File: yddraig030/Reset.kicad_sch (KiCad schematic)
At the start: 22 parts, among them J1301 ExtReset, J1302 Ext RUN LED, Q1301 2N4403, Q1302 2N4403, Q1303 2N4403, SW1301 Reset, U1301 NE555P

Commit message: ddraig030 schematic done
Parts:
- renumbered C1301 to C201, C1302 to C202, C1303 to C203, D1301 to D201, D1302 to D202, D1303 to D203, J1301 to J201, J1302 to J202, Q1301 to Q201, Q1302 to Q202, Q1303 to Q203, R1301 to R201, R1302 to R202, R1303 to R203, R1304 to R204, R1305 to R205, R1306 to R206, R1307 to R207, R1308 to R208, R1309 to R209, SW1301 to SW201, U1301 to U201

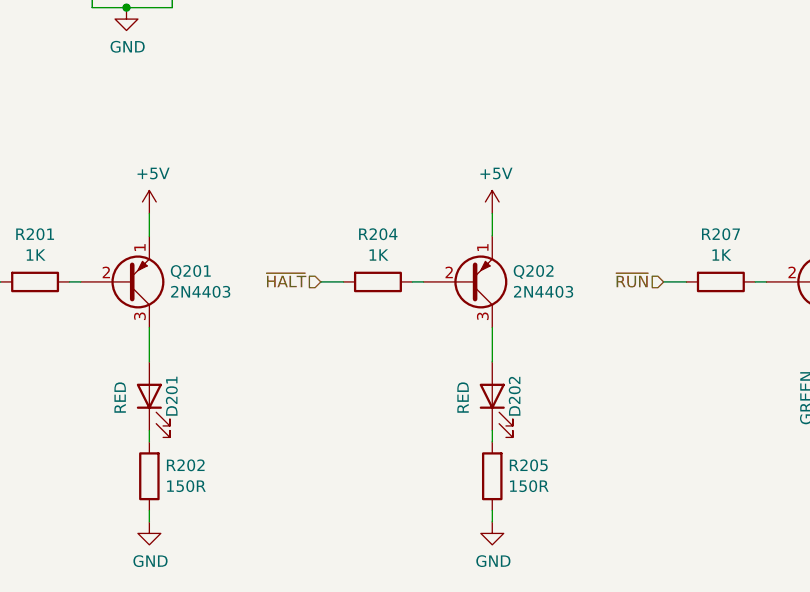
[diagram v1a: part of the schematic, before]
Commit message: yddraig030: Fixed ERC check errors
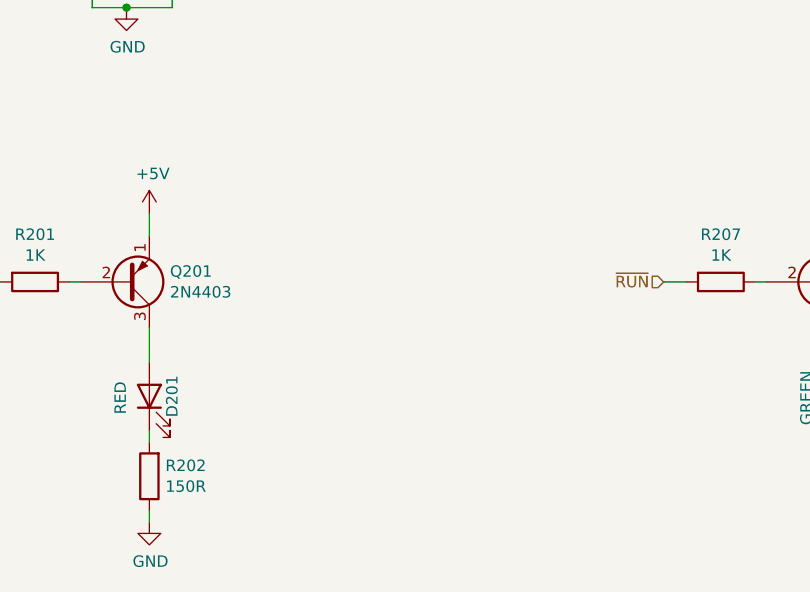
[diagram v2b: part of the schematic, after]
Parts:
- removed D202: RED, LED_THT:LED_D5.0mm, symbol Device:LED
- removed Q202: 2N4403, Package_TO_SOT_THT:TO-92, symbol Device:Q_PNP_EBC
- removed R204: 1K, Resistor_THT:R_Axial_DIN0207_L6.3mm_D2.5mm_P10.16mm_Horizontal, symbol Device:R
- removed R205: 150R, Resistor_THT:R_Axial_DIN0207_L6.3mm_D2.5mm_P10.16mm_Horizontal, symbol Device:R
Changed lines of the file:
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@@
-    (stroke (width 0) (type default) (color 0 0 0 0))
-  )
-  (wire (pts (xy 133.35 113.03) (xy 133.35 115.57))
     (stroke (width 0) (type default) (color 0 0 0 0))
   )
@@
     (stroke (width 0) (type default) (color 0 0 0 0))
   )
-  (wire (pts (xy 133.35 125.73) (xy 133.35 129.54))
-    (stroke (width 0) (type default) (color 0 0 0 0))
-  )
   (wire (pts (xy 135.89 77.47) (xy 152.4 77.47))
     (stroke (width 0) (type default) (color 0 0 0 0))
@@
     (stroke (width 0) (type default) (color 0 0 0 0))
   )
-  (wire (pts (xy 133.35 137.16) (xy 133.35 138.43))
-    (stroke (width 0) (type default) (color 0 0 0 0))
-  )
   (wire (pts (xy 95.25 125.73) (xy 95.25 129.54))
     (stroke (width 0) (type default) (color 0 0 0 0))
   )
-  (wire (pts (xy 114.3 120.65) (xy 116.84 120.65))
-    (stroke (width 0) (type default) (color 0 0 0 0))
-  )
   (wire (pts (xy 87.63 82.55) (xy 88.9 82.55))
     (stroke (width 0) (type default) (color 0 0 0 0))
@@
     (stroke (width 0) (type default) (color 0 0 0 0))
   )
-  (wire (pts (xy 124.46 120.65) (xy 125.73 120.65))
-    (stroke (width 0) (type default) (color 0 0 0 0))
-  )
   (wire (pts (xy 118.11 58.42) (xy 118.11 67.31))
     (stroke (width 0) (type default) (color 0 0 0 0))
@@
     (stroke (width 0) (type default) (color 0 0 0 0))
   )
-  (wire (pts (xy 133.35 146.05) (xy 133.35 147.32))
-    (stroke (width 0) (type default) (color 0 0 0 0))
-  )
   (wire (pts (xy 95.25 146.05) (xy 95.25 147.32))
     (stroke (width 0) (type default) (color 0 0 0 0))
-  )
-  (hierarchical_label "~{HALT}" (shape input) (at 114.3 120.65 180)
-    (effects (font (size 1.27 1.27)) (justify right))
   )
   (hierarchical_label "~{RUN}" (shape input) (at 152.4 120.65 180)
@@
       (effects (font (size 1.27 1.27)) hide)
     )
-    (pin "1")
-  )
-  (symbol (lib_id "Device:R") (at 120.65 120.65 270) (unit 1)
-    (in_bom yes) (on_board yes)
-    (property "Reference" "R204" (id 0) (at 120.65 115.3922 90))
-    (property "Value" "1K" (id 1) (at 120.65 117.7036 90))
-    (property "Footprint" "Resistor_THT:R_Axial_DIN0207_L6.3mm_D2.5mm_P10.16mm_Horizontal" (id 2) (at 120.65 118.872 90)
-      (effects (font (size 1.27 1.27)) hide)
-    )
-    (property "Datasheet" "~" (id 3) (at 120.65 120.65 0)
-      (effects (font (size 1.27 1.27)) hide)
-    )
-    (pin "1")
-    (pin "2")
-  )
-  (symbol (lib_id "Device:R") (at 133.35 142.24 180) (unit 1)
-    (in_bom yes) (on_board yes)
-    (property "Reference" "R205" (id 0) (at 135.128 141.0716 0)
-      (effects (font (size 1.27 1.27)) (justify right))
-    )
-    (property "Value" "150R" (id 1) (at 135.128 143.383 0)
-      (effects (font (size 1.27 1.27)) (justify right))
-    )
-    (property "Footprint" "Resistor_THT:R_Axial_DIN0207_L6.3mm_D2.5mm_P10.16mm_Horizontal" (id 2) (at 135.128 142.24 90)
-      (effects (font (size 1.27 1.27)) hide)
-    )
-    (property "Datasheet" "~" (id 3) (at 133.35 142.24 0)
-      (effects (font (size 1.27 1.27)) hide)
-    )
-    (pin "1")
-    (pin "2")
-  )
-  (symbol (lib_id "Device:Q_PNP_EBC") (at 130.81 120.65 0) (mirror x) (unit 1)
-    (in_bom yes) (on_board yes)
-    (property "Reference" "Q202" (id 0) (at 135.636 119.4816 0)
-      (effects (font (size 1.27 1.27)) (justify left))
-    )
-    (property "Value" "2N4403" (id 1) (at 135.636 121.793 0)
-      (effects (font (size 1.27 1.27)) (justify left))
-    )
-    (property "Footprint" "Package_TO_SOT_THT:TO-92" (id 2) (at 135.89 123.19 0)
-      (effects (font (size 1.27 1.27)) hide)
-    )
-    (property "Datasheet" "~" (id 3) (at 130.81 120.65 0)
-      (effects (font (size 1.27 1.27)) hide)
-    )
-    (pin "1")
-    (pin "2")
-    (pin "3")
-  )
-  (symbol (lib_id "Device:LED") (at 133.35 133.35 90) (unit 1)
-    (in_bom yes) (on_board yes)
-    (property "Reference" "D202" (id 0) (at 135.89 133.35 0))
-    (property "Value" "RED" (id 1) (at 130.1496 133.5278 0))
-    (property "Footprint" "LED_THT:LED_D5.0mm" (id 2) (at 133.35 133.35 0)
-      (effects (font (size 1.27 1.27)) hide)
-    )
-    (property "Datasheet" "~" (id 3) (at 133.35 133.35 0)
-      (effects (font (size 1.27 1.27)) hide)
-    )
-    (pin "1")
-    (pin "2")
-  )
-  (symbol (lib_id "power:GND") (at 133.35 147.32 0) (unit 1)
-    (in_bom yes) (on_board yes)
-    (property "Reference" "#PWR0205" (id 0) (at 133.35 153.67 0)
-      (effects (font (size 1.27 1.27)) hide)
-    )
-    (property "Value" "GND" (id 1) (at 133.477 151.7142 0))
-    (property "Footprint" "" (id 2) (at 133.35 147.32 0)
-      (effects (font (size 1.27 1.27)) hide)
-    )
-    (property "Datasheet" "" (id 3) (at 133.35 147.32 0)
-      (effects (font (size 1.27 1.27)) hide)
-    )
-    (pin "1")
-  )
-  (symbol (lib_id "power:+5V") (at 133.35 113.03 0) (unit 1)
-    (in_bom yes) (on_board yes)
-    (property "Reference" "#PWR0204" (id 0) (at 133.35 116.84 0)
-      (effects (font (size 1.27 1.27)) hide)
-    )
-    (property "Value" "+5V" (id 1) (at 133.731 108.6358 0))
-    (property "Footprint" "" (id 2) (at 133.35 113.03 0)
-      (effects (font (size 1.27 1.27)) hide)
-    )
-    (property "Datasheet" "" (id 3) (at 133.35 113.03 0)
-      (effects (font (size 1.27 1.27)) hide)
-    )

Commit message: Started PCB layout
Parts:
- renumbered D203 to D202, Q203 to Q202, R206 to R204, R207 to R205, R208 to R206, R209 to R207
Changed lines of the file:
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@@
   (symbol (lib_id "Device:R") (at 158.75 58.42 0) (unit 1)
     (in_bom yes) (on_board yes)
-    (property "Reference" "R206" (id 0) (at 160.528 57.2516 0)
+    (property "Reference" "R204" (id 0) (at 160.528 57.2516 0)
       (effects (font (size 1.27 1.27)) (justify left))
     )
@@
   (symbol (lib_id "power:GND") (at 135.89 80.01 0) (unit 1)
     (in_bom yes) (on_board yes)
-    (property "Reference" "#PWR0207" (id 0) (at 135.89 86.36 0)
+    (property "Reference" "#PWR0205" (id 0) (at 135.89 86.36 0)
       (effects (font (size 1.27 1.27)) hide)
     )
@@
   (symbol (lib_id "power:+5V") (at 135.89 43.18 0) (unit 1)
     (in_bom yes) (on_board yes)
-    (property "Reference" "#PWR0206" (id 0) (at 135.89 46.99 0)
+    (property "Reference" "#PWR0204" (id 0) (at 135.89 46.99 0)
       (effects (font (size 1.27 1.27)) hide)
     )
@@
   (symbol (lib_id "Device:R") (at 158.75 120.65 270) (unit 1)
     (in_bom yes) (on_board yes)
-    (property "Reference" "R207" (id 0) (at 158.75 115.3922 90))
+    (property "Reference" "R205" (id 0) (at 158.75 115.3922 90))
     (property "Value" "1K" (id 1) (at 158.75 117.7036 90))
     (property "Footprint" "Resistor_THT:R_Axial_DIN0207_L6.3mm_D2.5mm_P10.16mm_Horizontal" (id 2) (at 158.75 118.872 90)
@@
   (symbol (lib_id "Device:R") (at 171.45 142.24 180) (unit 1)
     (in_bom yes) (on_board yes)
-    (property "Reference" "R208" (id 0) (at 173.228 141.0716 0)
+    (property "Reference" "R206" (id 0) (at 173.228 141.0716 0)
       (effects (font (size 1.27 1.27)) (justify right))
     )
@@
   (symbol (lib_id "Device:Q_PNP_EBC") (at 168.91 120.65 0) (mirror x) (unit 1)
     (in_bom yes) (on_board yes)
-    (property "Reference" "Q203" (id 0) (at 173.736 119.4816 0)
+    (property "Reference" "Q202" (id 0) (at 173.736 119.4816 0)
       (effects (font (size 1.27 1.27)) (justify left))
     )
@@
   (symbol (lib_id "Device:LED") (at 171.45 133.35 90) (unit 1)
     (in_bom yes) (on_board yes)
-    (property "Reference" "D203" (id 0) (at 173.99 133.35 0))
+    (property "Reference" "D202" (id 0) (at 173.99 133.35 0))
     (property "Value" "GREEN" (id 1) (at 168.2496 133.5278 0))
     (property "Footprint" "LED_THT:LED_D5.0mm" (id 2) (at 171.45 133.35 0)
@@
   (symbol (lib_id "power:GND") (at 171.45 147.32 0) (unit 1)
     (in_bom yes) (on_board yes)
-    (property "Reference" "#PWR0209" (id 0) (at 171.45 153.67 0)
+    (property "Reference" "#PWR0207" (id 0) (at 171.45 153.67 0)
       (effects (font (size 1.27 1.27)) hide)
     )
@@
   (symbol (lib_id "power:+5V") (at 171.45 113.03 0) (unit 1)
     (in_bom yes) (on_board yes)
-    (property "Reference" "#PWR0208" (id 0) (at 171.45 116.84 0)
+    (property "Reference" "#PWR0206" (id 0) (at 171.45 116.84 0)
       (effects (font (size 1.27 1.27)) hide)
     )
@@
   (symbol (lib_id "Device:R") (at 184.15 142.24 180) (unit 1)
     (in_bom yes) (on_board yes)
-    (property "Reference" "R209" (id 0) (at 185.928 141.0716 0)
+    (property "Reference" "R207" (id 0) (at 185.928 141.0716 0)
       (effects (font (size 1.27 1.27)) (justify right))
     )
@@
   (symbol (lib_id "power:GND") (at 184.15 147.32 0) (unit 1)
     (in_bom yes) (on_board yes)
-    (property "Reference" "#PWR0210" (id 0) (at 184.15 153.67 0)
-      (effects (font (size 1.27 1.27)) hide)
-    )
+    (property "Reference" "#PWR0208" (id 0) (at 184.15 153.67 0)
+      (effects (font (size 1.27 1.27)) hide)
+    )

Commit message: Working on PCB layout
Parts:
- C201, C203: footprint Capacitor_THT:CP_Radial_D5.0mm_P2.50mm -> Capacitor_SMD:CP_Elec_4x5.3
- C202: footprint Capacitor_THT:C_Disc_D3.8mm_W2.6mm_P2.50mm -> Capacitor_SMD:C_0805_2012Metric
- D201, D202: footprint LED_THT:LED_D5.0mm -> LED_SMD:LED_1206_3216Metric
- R201, R202, R203, R204, R205, R206, R207: footprint Resistor_THT:R_Axial_DIN0207_L6.3mm_D2.5mm_P10.16mm_Horizontal -> Resistor_SMD:R_0805_2012Metric
- U201: footprint Package_DIP:DIP-8_W7.62mm -> Package_SO:SO-8_3.9x4.9mm_P1.27mm
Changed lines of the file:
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@@
     (property "Reference" "U201" (id 0) (at 130.81 48.26 0))
     (property "Value" "NE555P" (id 1) (at 140.97 48.26 0))
-    (property "Footprint" "Package_DIP:DIP-8_W7.62mm" (id 2) (at 152.4 68.58 0)
+    (property "Footprint" "Package_SO:SO-8_3.9x4.9mm_P1.27mm" (id 2) (at 152.4 68.58 0)
       (effects (font (size 1.27 1.27)) hide)
     )
@@
       (effects (font (size 1.27 1.27)) (justify left))
     )
-    (property "Footprint" "Resistor_THT:R_Axial_DIN0207_L6.3mm_D2.5mm_P10.16mm_Horizontal" (id 2) (at 104.902 58.42 90)
+    (property "Footprint" "Resistor_SMD:R_0805_2012Metric" (id 2) (at 104.902 58.42 90)
       (effects (font (size 1.27 1.27)) hide)
     )
@@
       (effects (font (size 1.27 1.27)) (justify left))
     )
-    (property "Footprint" "Resistor_THT:R_Axial_DIN0207_L6.3mm_D2.5mm_P10.16mm_Horizontal" (id 2) (at 156.972 58.42 90)
+    (property "Footprint" "Resistor_SMD:R_0805_2012Metric" (id 2) (at 156.972 58.42 90)
       (effects (font (size 1.27 1.27)) hide)
     )
@@
       (effects (font (size 1.27 1.27)) (justify left))
     )
-    (property "Footprint" "Capacitor_THT:CP_Radial_D5.0mm_P2.50mm" (id 2) (at 153.3652 74.93 0)
+    (property "Footprint" "Capacitor_SMD:CP_Elec_4x5.3" (id 2) (at 153.3652 74.93 0)
       (effects (font (size 1.27 1.27)) hide)
     )
@@
       (effects (font (size 1.27 1.27)) (justify left))
     )
-    (property "Footprint" "Capacitor_THT:CP_Radial_D5.0mm_P2.50mm" (id 2) (at 107.6452 74.93 0)
+    (property "Footprint" "Capacitor_SMD:CP_Elec_4x5.3" (id 2) (at 107.6452 74.93 0)
       (effects (font (size 1.27 1.27)) hide)
     )
@@
       (effects (font (size 1.27 1.27)) (justify left))
     )
-    (property "Footprint" "Capacitor_THT:C_Disc_D3.8mm_W2.6mm_P2.50mm" (id 2) (at 119.0752 74.93 0)
+    (property "Footprint" "Capacitor_SMD:C_0805_2012Metric" (id 2) (at 119.0752 74.93 0)
       (effects (font (size 1.27 1.27)) hide)
     )
@@
     (property "Reference" "R201" (id 0) (at 82.55 115.3922 90))
     (property "Value" "1K" (id 1) (at 82.55 117.7036 90))
-    (property "Footprint" "Resistor_THT:R_Axial_DIN0207_L6.3mm_D2.5mm_P10.16mm_Horizontal" (id 2) (at 82.55 118.872 90)
+    (property "Footprint" "Resistor_SMD:R_0805_2012Metric" (id 2) (at 82.55 118.872 90)
       (effects (font (size 1.27 1.27)) hide)
     )
@@
       (effects (font (size 1.27 1.27)) (justify right))
     )
-    (property "Footprint" "Resistor_THT:R_Axial_DIN0207_L6.3mm_D2.5mm_P10.16mm_Horizontal" (id 2) (at 97.028 142.24 90)
+    (property "Footprint" "Resistor_SMD:R_0805_2012Metric" (id 2) (at 97.028 142.24 90)
       (effects (font (size 1.27 1.27)) hide)
     )
@@
     (property "Reference" "D201" (id 0) (at 97.79 133.35 0))
     (property "Value" "RED" (id 1) (at 92.0496 133.5278 0))
-    (property "Footprint" "LED_THT:LED_D5.0mm" (id 2) (at 95.25 133.35 0)
+    (property "Footprint" "LED_SMD:LED_1206_3216Metric" (id 2) (at 95.25 133.35 0)
       (effects (font (size 1.27 1.27)) hide)
     )
@@
     (property "Reference" "R205" (id 0) (at 158.75 115.3922 90))
     (property "Value" "1K" (id 1) (at 158.75 117.7036 90))
-    (property "Footprint" "Resistor_THT:R_Axial_DIN0207_L6.3mm_D2.5mm_P10.16mm_Horizontal" (id 2) (at 158.75 118.872 90)
+    (property "Footprint" "Resistor_SMD:R_0805_2012Metric" (id 2) (at 158.75 118.872 90)
       (effects (font (size 1.27 1.27)) hide)
     )
@@
       (effects (font (size 1.27 1.27)) (justify right))
     )
-    (property "Footprint" "Resistor_THT:R_Axial_DIN0207_L6.3mm_D2.5mm_P10.16mm_Horizontal" (id 2) (at 173.228 142.24 90)
+    (property "Footprint" "Resistor_SMD:R_0805_2012Metric" (id 2) (at 173.228 142.24 90)
       (effects (font (size 1.27 1.27)) hide)
     )
@@
     (property "Reference" "D202" (id 0) (at 173.99 133.35 0))
     (property "Value" "GREEN" (id 1) (at 168.2496 133.5278 0))
-    (property "Footprint" "LED_THT:LED_D5.0mm" (id 2) (at 171.45 133.35 0)
+    (property "Footprint" "LED_SMD:LED_1206_3216Metric" (id 2) (at 171.45 133.35 0)
       (effects (font (size 1.27 1.27)) hide)
     )
@@
       (effects (font (size 1.27 1.27)) (justify right))
     )
-    (property "Footprint" "Resistor_THT:R_Axial_DIN0207_L6.3mm_D2.5mm_P10.16mm_Horizontal" (id 2) (at 185.928 142.24 90)
-      (effects (font (size 1.27 1.27)) hide)
-    )
+    (property "Footprint" "Resistor_SMD:R_0805_2012Metric" (id 2) (at 185.928 142.24 90)
+      (effects (font (size 1.27 1.27)) hide)
+    )

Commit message: Some more changes to SMD version
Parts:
- removed Q201, Q202: 2N4403, Package_TO_SOT_THT:TO-92, symbol Device:Q_PNP_EBC
- added Q201, Q202: BC858, Package_TO_SOT_SMD:SOT-23, symbol Transistor_BJT:BC858
- U201: footprint Package_SO:SO-8_3.9x4.9mm_P1.27mm -> Package_SO:SO-8_5.3x6.2mm_P1.27mm
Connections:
- net +5V: now also Q201.2 (E), Q202.2 (E)
- net at R201.1: now also Q201.1 (B)
- net at D201.2 (A): now also Q201.3 (C)
- net at R205.1: now also Q202.1 (B)
- net at D202.2 (A), J202.1 (Pin_1): now also Q202.3 (C)
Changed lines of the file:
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@@
     (property "Reference" "U201" (id 0) (at 130.81 48.26 0))
     (property "Value" "NE555P" (id 1) (at 140.97 48.26 0))
-    (property "Footprint" "Package_SO:SO-8_3.9x4.9mm_P1.27mm" (id 2) (at 152.4 68.58 0)
+    (property "Footprint" "Package_SO:SO-8_5.3x6.2mm_P1.27mm" (id 2) (at 152.4 68.58 0)
       (effects (font (size 1.27 1.27)) hide)
     )
@@
     (pin "2")
   )
-  (symbol (lib_id "Device:Q_PNP_EBC") (at 92.71 120.65 0) (mirror x) (unit 1)
-    (in_bom yes) (on_board yes)
-    (property "Reference" "Q201" (id 0) (at 97.536 119.4816 0)
-      (effects (font (size 1.27 1.27)) (justify left))
-    )
-    (property "Value" "2N4403" (id 1) (at 97.536 121.793 0)
-      (effects (font (size 1.27 1.27)) (justify left))
-    )
-    (property "Footprint" "Package_TO_SOT_THT:TO-92" (id 2) (at 97.79 123.19 0)
-      (effects (font (size 1.27 1.27)) hide)
-    )
-    (property "Datasheet" "~" (id 3) (at 92.71 120.65 0)
-      (effects (font (size 1.27 1.27)) hide)
-    )
-    (pin "1")
-    (pin "2")
-    (pin "3")
-  )
   (symbol (lib_id "Device:LED") (at 95.25 133.35 90) (unit 1)
     (in_bom yes) (on_board yes)
@@
     (pin "2")
   )
-  (symbol (lib_id "Device:Q_PNP_EBC") (at 168.91 120.65 0) (mirror x) (unit 1)
-    (in_bom yes) (on_board yes)
-    (property "Reference" "Q202" (id 0) (at 173.736 119.4816 0)
-      (effects (font (size 1.27 1.27)) (justify left))
-    )
-    (property "Value" "2N4403" (id 1) (at 173.736 121.793 0)
-      (effects (font (size 1.27 1.27)) (justify left))
-    )
-    (property "Footprint" "Package_TO_SOT_THT:TO-92" (id 2) (at 173.99 123.19 0)
-      (effects (font (size 1.27 1.27)) hide)
-    )
-    (property "Datasheet" "~" (id 3) (at 168.91 120.65 0)
-      (effects (font (size 1.27 1.27)) hide)
-    )
-    (pin "1")
-    (pin "2")
-    (pin "3")
-  )
   (symbol (lib_id "Device:LED") (at 171.45 133.35 90) (unit 1)
     (in_bom yes) (on_board yes)
@@
     (pin "1")
   )
+  (symbol (lib_id "Transistor_BJT:BC858") (at 92.71 120.65 0) (mirror x) (unit 1)
+    (in_bom yes) (on_board yes) (fields_autoplaced)
+    (property "Reference" "Q201" (id 0) (at 98.044 119.3799 0)
+      (effects (font (size 1.27 1.27)) (justify left))
+    )
+    (property "Value" "BC858" (id 1) (at 98.044 121.9199 0)
+      (effects (font (size 1.27 1.27)) (justify left))
+    )
+    (property "Footprint" "Package_TO_SOT_SMD:SOT-23" (id 2) (at 97.79 118.745 0)
+      (effects (font (size 1.27 1.27) italic) (justify left) hide)
+    )
+    (property "Datasheet" "https://www.onsemi.com/pub/Collateral/BC860-D.pdf" (id 3) (at 92.71 120.65 0)
+      (effects (font (size 1.27 1.27)) (justify left) hide)
+    )
+    (pin "1")
+    (pin "2")
+    (pin "3")
+  )
+  (symbol (lib_id "Transistor_BJT:BC858") (at 168.91 120.65 0) (mirror x) (unit 1)
+    (in_bom yes) (on_board yes) (fields_autoplaced)
+    (property "Reference" "Q202" (id 0) (at 174.244 119.3799 0)
+      (effects (font (size 1.27 1.27)) (justify left))
+    )
+    (property "Value" "BC858" (id 1) (at 174.244 121.9199 0)
+      (effects (font (size 1.27 1.27)) (justify left))
+    )
+    (property "Footprint" "Package_TO_SOT_SMD:SOT-23" (id 2) (at 173.99 118.745 0)
+      (effects (font (size 1.27 1.27) italic) (justify left) hide)
+    )
+    (property "Datasheet" "https://www.onsemi.com/pub/Collateral/BC860-D.pdf" (id 3) (at 168.91 120.65 0)
+      (effects (font (size 1.27 1.27)) (justify left) hide)
+    )
+    (pin "1")
+    (pin "2")
+    (pin "3")
+  )
 )
